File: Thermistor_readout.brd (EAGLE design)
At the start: 90 x 60 mm, 25 parts, among them Q1 BC550C, U1 TI_NATIONAL_SEMICONDUCTOR_LF3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, U2 TI_NATIONAL_SEMICONDUCTOR_LF3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, U3 ANALOG_DEVICES_ADG725BSUZANAL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, U4 TI_NATIONAL_SEMICONDUCTOR_LF3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

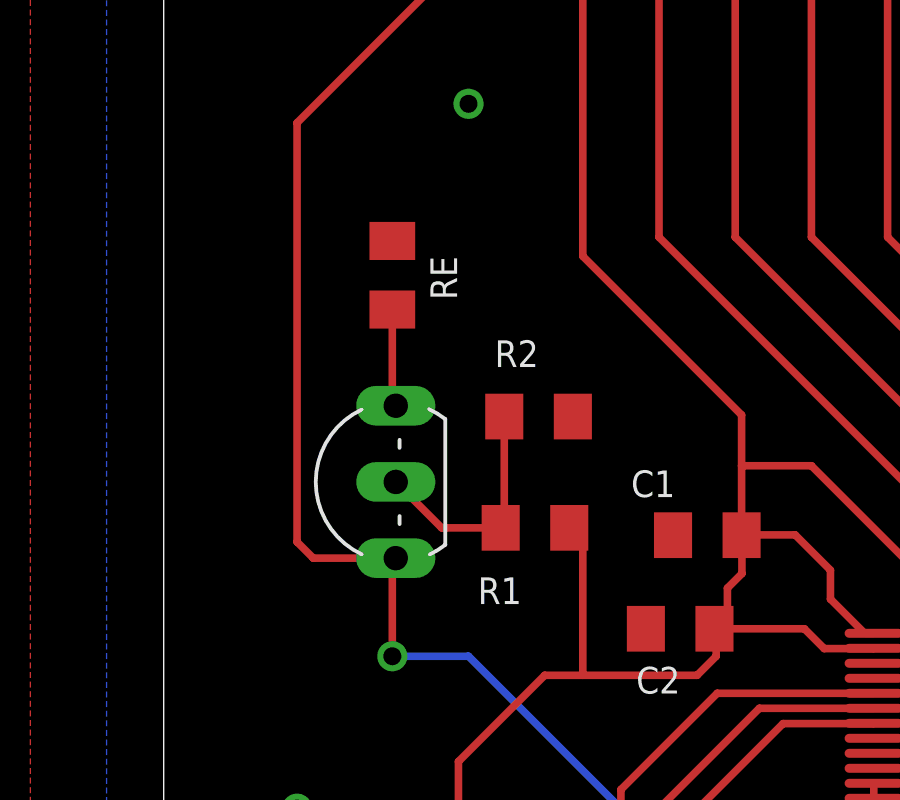
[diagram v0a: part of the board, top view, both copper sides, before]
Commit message: double sized Re resistor
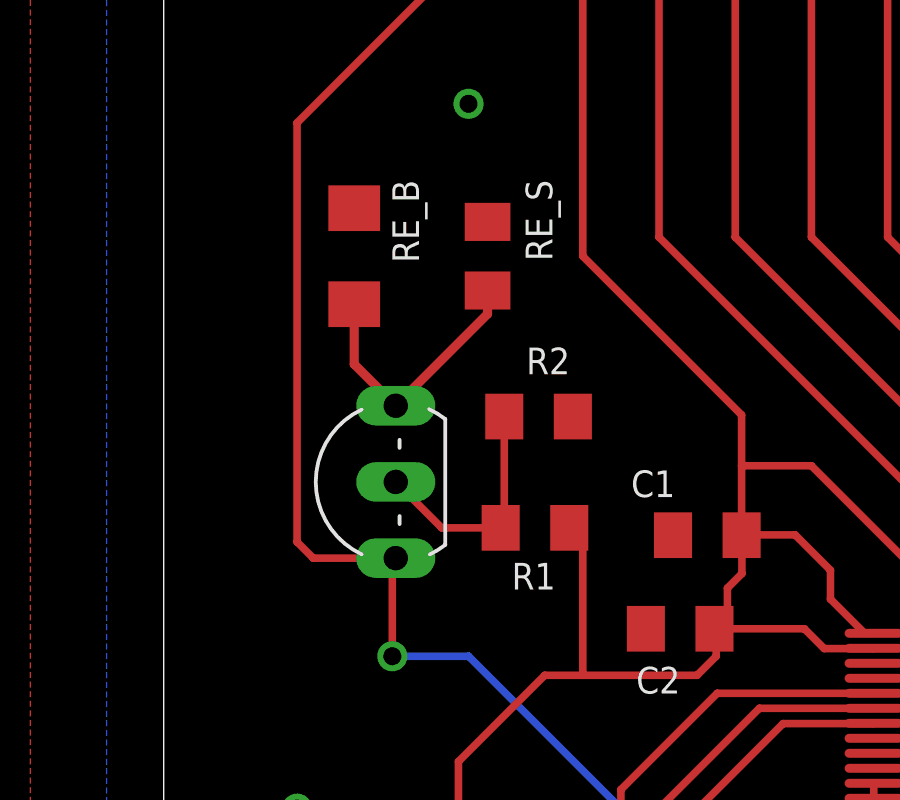
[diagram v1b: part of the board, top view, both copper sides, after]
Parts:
- removed RE: (no value), 1AKarstenLib:R0805H
- added RE_B: 15kΩ, 1AKarstenLib:R1206H
- added RE_S: 1.5kΩ, 1AKarstenLib:R0805H
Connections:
- net GND: now also RE_B.1, RE_S.1; no longer RE.1
- net N$2: now also RE_B.2, RE_S.2; no longer RE.2
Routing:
- net N$2: track 3.40 -> 9.07 mm
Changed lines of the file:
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@@
 <drawing>
 <settings>
-<setting alwaysvectorfont="no"/>
+<setting alwaysvectorfont="yes"/>
 <setting verticaltext="up"/>
 </settings>
@@
 <layers>
 <layer number="1" name="Top" color="4" fill="1" visible="yes" active="yes"/>
+<layer number="2" name="Route2" color="1" fill="3" visible="yes" active="yes"/>
+<layer number="3" name="Route3" color="4" fill="3" visible="yes" active="yes"/>
+<layer number="4" name="Route4" color="1" fill="4" visible="yes" active="yes"/>
+<layer number="5" name="Route5" color="4" fill="4" visible="yes" active="yes"/>
+<layer number="6" name="Route6" color="1" fill="8" visible="yes" active="yes"/>
+<layer number="7" name="Route7" color="4" fill="8" visible="yes" active="yes"/>
+<layer number="8" name="Route8" color="1" fill="2" visible="yes" active="yes"/>
+<layer number="9" name="Route9" color="4" fill="2" visible="yes" active="yes"/>
+<layer number="10" name="Route10" color="1" fill="7" visible="yes" active="yes"/>
+<layer number="11" name="Route11" color="4" fill="7" visible="yes" active="yes"/>
+<layer number="12" name="Route12" color="1" fill="5" visible="yes" active="yes"/>
+<layer number="13" name="Route13" color="4" fill="5" visible="yes" active="yes"/>
+<layer number="14" name="Route14" color="1" fill="6" visible="yes" active="yes"/>
+<layer number="15" name="Route15" color="4" fill="6" visible="yes" active="yes"/>
 <layer number="16" name="Bottom" color="1" fill="1" visible="yes" active="yes"/>
 <layer number="17" name="Pads" color="2" fill="1" visible="yes" active="yes"/>
@@
 </element>
 <element name="R1" library="1AKarstenLib" package="R0805H" value="1.1ΜΩ" x="12.375" y="30.315" smashed="yes">
-<attribute name="NAME" x="10.47" y="27.775" size="0.889" layer="25"/>
+<attribute name="NAME" x="11.59903125" y="28.258871875" size="0.889" layer="25"/>
 </element>
 <element name="R2" library="1AKarstenLib" package="R0805H" value="1ΜΩ" x="12.495" y="34.025" smashed="yes" rot="R180">
-<attribute name="NAME" x="12.495" y="36.565" size="0.889" layer="25" rot="R180"/>
+<attribute name="NAME" x="13.543384375" y="36.323065625" size="0.889" layer="25" rot="R180"/>
 </element>
 <element name="R4" library="1AKarstenLib" package="R0805H" value="1kΩ" x="68.63" y="51.07" smashed="yes">
@@
 <attribute name="VALUE" x="41.275" y="10.16" size="1.27" layer="27" rot="R180"/>
 </element>
-<element name="RE" library="1AKarstenLib" package="R0805H" value="" x="7.62" y="38.735" smashed="yes" rot="R270">
-<attribute name="NAME" x="8.89" y="39.37" size="0.889" layer="25" rot="R270"/>
-<attribute name="VALUE" x="6.985" y="36.195" size="1.27" layer="27" rot="R270"/>
+<element name="RE_B" library="1AKarstenLib" package="R1206H" value="15kΩ" x="6.35" y="39.37" smashed="yes" rot="R270">
+<attribute name="NAME" x="7.62" y="41.91" size="0.889" layer="25" rot="R270"/>
+<attribute name="VALUE" x="5.715" y="36.195" size="1.27" layer="27" rot="R270"/>
+</element>
+<element name="RE_S" library="1AKarstenLib" package="R0805H" value="1.5kΩ" x="10.795" y="39.37" smashed="yes" rot="R270">
+<attribute name="NAME" x="12.065" y="41.91" size="0.889" layer="25" rot="R270"/>
+<attribute name="VALUE" x="10.16" y="36.83" size="1.27" layer="27" rot="R270"/>
 </element>
 </elements>
@@
 <signal name="N$2">
 <contactref element="Q1" pad="E"/>
-<wire x1="7.515" y1="34.605" x2="7.735" y2="34.385" width="0.254" layer="1"/>
-<contactref element="RE" pad="2"/>
-<wire x1="7.515" y1="34.605" x2="7.62" y2="34.605" width="0.254" layer="1"/>
-<wire x1="7.62" y1="34.605" x2="7.62" y2="37.592" width="0.254" layer="1"/>
+<contactref element="RE_B" pad="2"/>
+<contactref element="RE_S" pad="2"/>
+<wire x1="6.35" y1="37.7698" x2="6.35" y2="35.77" width="0.3048" layer="1"/>
+<wire x1="6.35" y1="35.77" x2="7.735" y2="34.385" width="0.3048" layer="1"/>
+<wire x1="10.795" y1="38.227" x2="10.795" y2="37.445" width="0.3048" layer="1"/>
+<wire x1="10.795" y1="37.445" x2="7.735" y2="34.385" width="0.3048" layer="1"/>
 </signal>
 <signal name="N$24">
@@
 <contactref element="CON1" pad="15"/>
 <via x="4.445" y="20.955" extent="1-16" drill="0.6" shape="square"/>
-<contactref element="RE" pad="1"/>
 <polygon width="0.4064" layer="1">
 <vertex x="-4.445" y="62.865"/>
@@
 <vertex x="-1.905" y="60.96"/>
 </polygon>
+<contactref element="RE_B" pad="1"/>
+<contactref element="RE_S" pad="1"/>
 </signal>
 <signal name="+5V">

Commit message: 1206_capacitors
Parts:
- C1, C2, C3, C4, C5, C6, C7, C8: device 1AKarstenLib:R0805H -> 1AKarstenLib:R1206H
- moved CON1 1.61 mm to (32.7, 3.81)
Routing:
- net -15V: track 107.6 -> 105.3 mm
- net +5V: track 93.1 -> 95.3 mm
- net +15V: track 94.0 -> 95.3 mm
- net N$13: track 29.2 -> 29.8 mm
- net N$14: track 27.8 -> 28.5 mm
- net N$11: track 26.9 -> 27.5 mm
- net N$24: track 92.5 -> 91.9 mm
